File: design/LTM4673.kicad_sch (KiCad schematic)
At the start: 96 parts, among them U35 LTM4673IY#PBF

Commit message: BOM adjustments for LTM4673 feedback resistors
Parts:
- R217: Manufacturer Part Number ERJ-PB3B9092V -> R0603_90K9_0.1%_0.20W_50PPM; Manufacturer1 ComponentHeight 0.4mm -> 0.65mm; Part Description Thin Film Precision Resistor -> Thick Film Precision Resistor; Part Number R0402_90K9_0.1%_0.063W_25PPM -> R0603_90K9_0.1%_0.20W_50PPM; Power 0.063W -> 0.20W; TC ±25ppm/°C -> ±50ppm/°C; Voltage 50V -> (none)
- R219: Manufacturer Part Number ERJ-PB3B1332V -> R0603_13K3_0.1%_0.20W_50PPM; Manufacturer1 ComponentHeight 0.5mm -> 0.65mm; Manufacturer1 Example TYCO HOLSWORTHY -> PANASONIC; Manufacturer1 Part Number ERJ-PB3B1332V -> ERJ-PB3B1332V; Part Description Thin Film Chip Resistor -> Thick Film Precision Resistor; Part Number R0603_13K3_0.1%_0.063W_10PPM -> R0603_13K3_0.1%_0.20W_50PPM; Power 0.063W -> 0.20W; TC ±10ppm -> ±50ppm/°C
- R220: Manufacturer Part Number ERJ-PB3B3002V -> R0603_30K0_0.1%_0.20W_50PPM; Manufacturer1 ComponentHeight 0.5mm -> 0.65mm; Manufacturer1 Example TYCO HOLSWORTHY -> PANASONIC; Manufacturer1 Part Number ERJ-PB3B3002V -> ERJ-PB3B3002V; Part Description Thin Film Chip Resistor -> Thick Film Precision Resistor; Part Number R0603_30K0_0.1%_0.063W_10PPM -> R0603_30K0_0.1%_0.20W_50PPM; Power 0.063W -> 0.20W; TC ±10ppm -> ±50ppm/°C
- R226: Manufacturer Part Number R0603_19K1_0.1%_0.063W_25PPM -> R0603_19K1_0.1%_0.20W_50PPM; Manufacturer1 ComponentHeight 0.35mm -> 0.65mm; Manufacturer1 Example TE CONNECTIVITY -> PANASONIC; Manufacturer1 Part Number ERJ-PB3B1912V -> ERJ-PB3B1912V; Part Description Thin Film Precision Resistor -> Thick Film Precision Resistor; Part Number ERJ-PB3B1912V -> R0603_19K1_0.1%_0.20W_50PPM; Power 0.063W -> 0.20W; TC ±25ppm/°C -> ±50ppm/°C
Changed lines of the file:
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@@
       (effects (font (size 0.8 0.8)))
     )
-    (property "Part Number" "R0603_13K3_0.1%_0.063W_10PPM" (id 5) (at 244.602 225.552 0)
+    (property "Part Number" "R0603_13K3_0.1%_0.20W_50PPM" (id 5) (at 244.602 225.552 0)
       (effects (font (size 1.27 1.27)) (justify left bottom) hide)
     )
@@
       (effects (font (size 1.27 1.27)) (justify left bottom) hide)
     )
-    (property "Power" "0.063W" (id 12) (at 244.602 225.552 0)
+    (property "Power" "0.20W" (id 12) (at 244.602 225.552 0)
       (effects (font (size 1.27 1.27)) (justify left bottom) hide)
     )
-    (property "TC" "±10ppm" (id 13) (at 244.602 225.552 0)
+    (property "TC" "±50ppm/°C" (id 13) (at 244.602 225.552 0)
       (effects (font (size 1.27 1.27)) (justify left bottom) hide)
     )
-    (property "Part Description" "Thin Film Chip Resistor" (id 14) (at 244.602 225.552 0)
+    (property "Part Description" "Thick Film Precision Resistor" (id 14) (at 244.602 225.552 0)
       (effects (font (size 1.27 1.27)) (justify left bottom) hide)
     )
@@
       (effects (font (size 1.27 1.27)) (justify left bottom) hide)
     )
-    (property "Manufacturer1 Example" "TYCO HOLSWORTHY" (id 23) (at 244.602 225.552 0)
+    (property "Manufacturer1 Example" "PANASONIC" (id 23) (at 244.602 225.552 0)
       (effects (font (size 1.27 1.27)) (justify left bottom) hide)
     )
-    (property "Manufacturer1 Part Number" " ERJ-PB3B1332V" (id 24) (at 244.602 225.552 0)
+    (property "Manufacturer1 Part Number" "ERJ-PB3B1332V" (id 24) (at 244.602 225.552 0)
       (effects (font (size 1.27 1.27)) (justify left bottom) hide)
     )
-    (property "Manufacturer1 ComponentHeight" "0.5mm" (id 25) (at 244.602 225.552 0)
+    (property "Manufacturer1 ComponentHeight" "0.65mm" (id 25) (at 244.602 225.552 0)
       (effects (font (size 1.27 1.27)) (justify left bottom) hide)
     )
@@
       (effects (font (size 1.27 1.27)) (justify left bottom) hide)
     )
-    (property "Manufacturer Part Number" " ERJ-PB3B1332V" (id 30) (at 245.11 228.6 0)
+    (property "Manufacturer Part Number" "R0603_13K3_0.1%_0.20W_50PPM" (id 30) (at 245.11 228.6 0)
       (effects (font (size 1.27 1.27)) hide)
     )
@@
       (effects (font (size 0.8 0.8)))
     )
-    (property "Part Number" "R0603_30K0_0.1%_0.063W_10PPM" (id 5) (at 251.714 116.332 0)
+    (property "Part Number" "R0603_30K0_0.1%_0.20W_50PPM" (id 5) (at 251.714 116.332 0)
       (effects (font (size 1.27 1.27)) (justify left bottom) hide)
     )
@@
       (effects (font (size 1.27 1.27)) (justify left bottom) hide)
     )
-    (property "Power" "0.063W" (id 12) (at 251.714 116.332 0)
+    (property "Power" "0.20W" (id 12) (at 251.714 116.332 0)
       (effects (font (size 1.27 1.27)) (justify left bottom) hide)
     )
-    (property "TC" "±10ppm" (id 13) (at 251.714 116.332 0)
+    (property "TC" "±50ppm/°C" (id 13) (at 251.714 116.332 0)
       (effects (font (size 1.27 1.27)) (justify left bottom) hide)
     )
-    (property "Part Description" "Thin Film Chip Resistor" (id 14) (at 251.714 116.332 0)
+    (property "Part Description" "Thick Film Precision Resistor" (id 14) (at 251.714 116.332 0)
       (effects (font (size 1.27 1.27)) (justify left bottom) hide)
     )
@@
       (effects (font (size 1.27 1.27)) (justify left bottom) hide)
     )
-    (property "Manufacturer1 Example" "TYCO HOLSWORTHY" (id 23) (at 251.714 116.332 0)
+    (property "Manufacturer1 Example" "PANASONIC" (id 23) (at 251.714 116.332 0)
       (effects (font (size 1.27 1.27)) (justify left bottom) hide)
     )
-    (property "Manufacturer1 Part Number" " ERJ-PB3B3002V" (id 24) (at 251.714 116.332 0)
+    (property "Manufacturer1 Part Number" "ERJ-PB3B3002V" (id 24) (at 251.714 116.332 0)
       (effects (font (size 1.27 1.27)) (justify left bottom) hide)
     )
-    (property "Manufacturer1 ComponentHeight" "0.5mm" (id 25) (at 251.714 116.332 0)
+    (property "Manufacturer1 ComponentHeight" "0.65mm" (id 25) (at 251.714 116.332 0)
       (effects (font (size 1.27 1.27)) (justify left bottom) hide)
     )
@@
       (effects (font (size 1.27 1.27)) (justify left bottom) hide)
     )
-    (property "Manufacturer Part Number" " ERJ-PB3B3002V" (id 30) (at 252.73 124.46 0)
+    (property "Manufacturer Part Number" "R0603_30K0_0.1%_0.20W_50PPM" (id 30) (at 252.73 124.46 0)
       (effects (font (size 1.27 1.27)) hide)
     )
@@
       (effects (font (size 0.8 0.8)))
     )
-    (property "Part Number" " ERJ-PB3B1912V" (id 5) (at 251.714 162.052 0)
+    (property "Part Number" "R0603_19K1_0.1%_0.20W_50PPM" (id 5) (at 251.714 162.052 0)
       (effects (font (size 1.27 1.27)) (justify left bottom) hide)
     )
@@
       (effects (font (size 1.27 1.27)) (justify left bottom) hide)
     )
-    (property "Power" "0.063W" (id 12) (at 251.714 162.052 0)
+    (property "Power" "0.20W" (id 12) (at 251.714 162.052 0)
       (effects (font (size 1.27 1.27)) (justify left bottom) hide)
     )
-    (property "TC" "±25ppm/°C" (id 13) (at 251.714 162.052 0)
+    (property "TC" "±50ppm/°C" (id 13) (at 251.714 162.052 0)
       (effects (font (size 1.27 1.27)) (justify left bottom) hide)
     )
-    (property "Part Description" "Thin Film Precision Resistor" (id 14) (at 251.714 162.052 0)
+    (property "Part Description" "Thick Film Precision Resistor" (id 14) (at 251.714 162.052 0)
       (effects (font (size 1.27 1.27)) (justify left bottom) hide)
     )
@@
       (effects (font (size 1.27 1.27)) (justify left bottom) hide)
     )
-    (property "Manufacturer1 Example" "TE CONNECTIVITY" (id 23) (at 251.714 162.052 0)
+    (property "Manufacturer1 Example" "PANASONIC" (id 23) (at 251.714 162.052 0)
       (effects (font (size 1.27 1.27)) (justify left bottom) hide)
     )
-    (property "Manufacturer1 Part Number" " ERJ-PB3B1912V" (id 24) (at 251.714 162.052 0)
+    (property "Manufacturer1 Part Number" "ERJ-PB3B1912V" (id 24) (at 251.714 162.052 0)
       (effects (font (size 1.27 1.27)) (justify left bottom) hide)
     )
-    (property "Manufacturer1 ComponentHeight" "0.35mm" (id 25) (at 251.714 162.052 0)
+    (property "Manufacturer1 ComponentHeight" "0.65mm" (id 25) (at 251.714 162.052 0)
       (effects (font (size 1.27 1.27)) (justify left bottom) hide)
     )
@@
       (effects (font (size 1.27 1.27)) (justify left bottom) hide)
     )
-    (property "Manufacturer Part Number" "R0603_19K1_0.1%_0.063W_25PPM" (id 30) (at 252.73 170.18 0)
+    (property "Manufacturer Part Number" "R0603_19K1_0.1%_0.20W_50PPM" (id 30) (at 252.73 170.18 0)
       (effects (font (size 1.27 1.27)) hide)
     )
@@
       (effects (font (size 0.8 0.8)))
     )
-    (property "Part Number" "R0402_90K9_0.1%_0.063W_25PPM" (id 5) (at 244.602 65.532 0)
+    (property "Part Number" "R0603_90K9_0.1%_0.20W_50PPM" (id 5) (at 244.602 65.532 0)
       (effects (font (size 1.27 1.27)) (justify left bottom) hide)
     )
@@
       (effects (font (size 1.27 1.27)) (justify left bottom) hide)
     )
-    (property "Power" "0.063W" (id 12) (at 244.602 65.532 0)
+    (property "Power" "0.20W" (id 12) (at 244.602 65.532 0)
       (effects (font (size 1.27 1.27)) (justify left bottom) hide)
     )
-    (property "TC" "±25ppm/°C" (id 13) (at 244.602 65.532 0)
+    (property "TC" "±50ppm/°C" (id 13) (at 244.602 65.532 0)
       (effects (font (size 1.27 1.27)) (justify left bottom) hide)
     )
-    (property "Voltage" "50V" (id 14) (at 244.602 65.532 0)
-      (effects (font (size 1.27 1.27)) (justify left bottom) hide)
-    )
-    (property "Part Description" "Thin Film Precision Resistor" (id 15) (at 244.602 65.532 0)
+    (property "Part Description" "Thick Film Precision Resistor" (id 15) (at 244.602 65.532 0)
       (effects (font (size 1.27 1.27)) (justify left bottom) hide)
     )
@@
       (effects (font (size 1.27 1.27)) (justify left bottom) hide)
     )
-    (property "Manufacturer1 ComponentHeight" "0.4mm" (id 26) (at 244.602 65.532 0)
+    (property "Manufacturer1 ComponentHeight" "0.65mm" (id 26) (at 244.602 65.532 0)
       (effects (font (size 1.27 1.27)) (justify left bottom) hide)
     )
@@
       (effects (font (size 1.27 1.27)) (justify left bottom) hide)
     )
-    (property "Manufacturer Part Number" "ERJ-PB3B9092V" (id 31) (at 245.11 68.58 0)
+    (property "Manufacturer Part Number" "R0603_90K9_0.1%_0.20W_50PPM" (id 31) (at 245.11 68.58 0)
       (effects (font (size 1.27 1.27)) hide)
     )

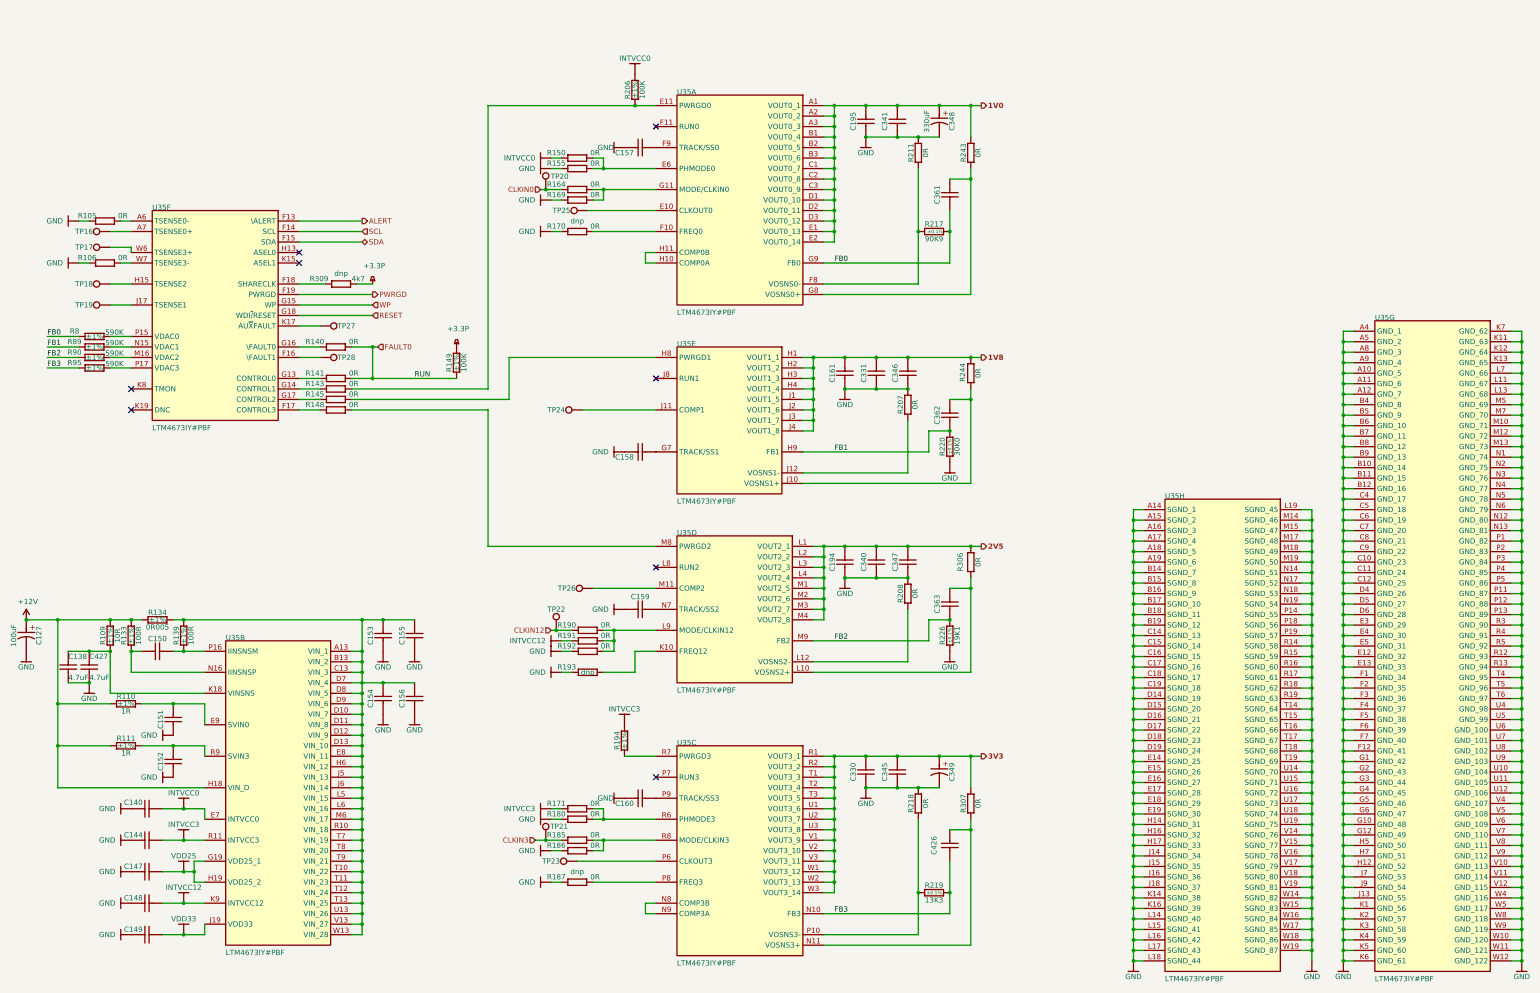
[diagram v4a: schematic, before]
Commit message: Fix duplicate parts in BOM and add missingpart numbers to some
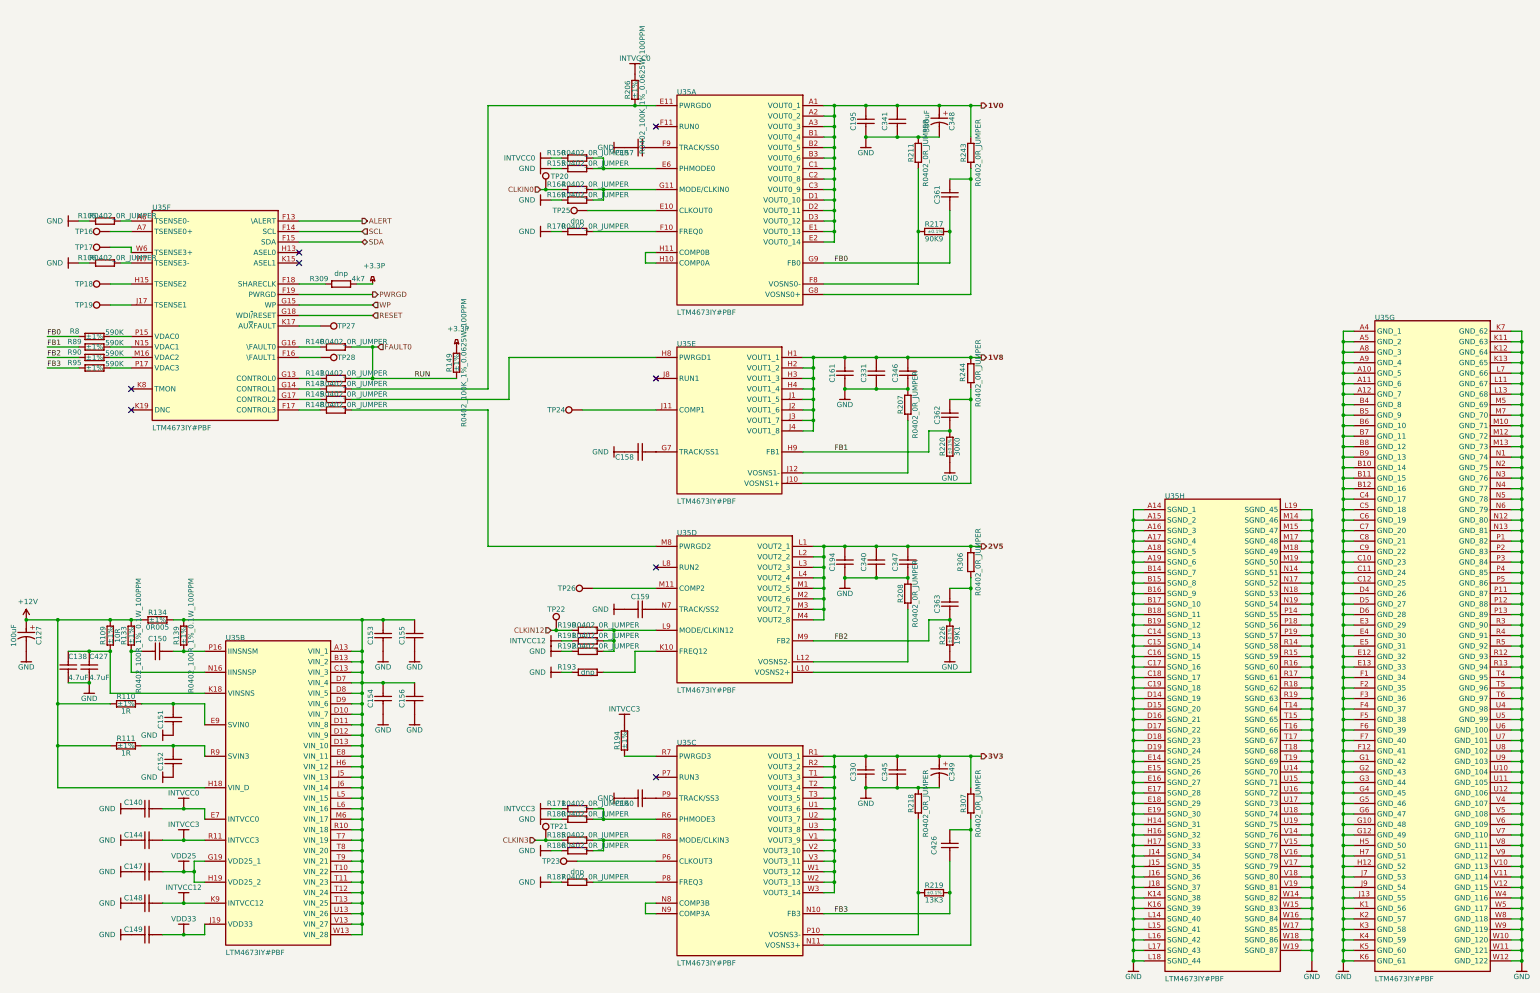
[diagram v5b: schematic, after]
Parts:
- R105, R106, R140, R141, R143, R145, R148, R150, R155, R164, R169, R170, R171, R180, R185, R186, R187, R190, R191, R192, R207, R208, R211, R218, R243, R244, R306, R307: value 0R -> R0402_0R_JUMPER
- R133, R139: value 100R -> R0402_100R_1%_0.1W_100PPM
- R149, R206: value 100K -> R0402_100K_1%_0.0625W_100PPM
